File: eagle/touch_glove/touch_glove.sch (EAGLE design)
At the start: 0 parts

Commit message: Added PWM driver and DEMUX to both robotic arm and touch glove.  Added some transistors to touch glove
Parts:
- added C1: CAP_CER_SMD-805_0.1UF-50V-10%, MrSwirlyEyes:CAP_CER_SMD-805_0.1UF-50V-10%
- added C2: CAP_CER_SMD-805_10UF-25V-10%, MrSwirlyEyes:CAP_CER_SMD-805_10UF-25V-10%
- added DEMUX: CD74HC4067-SM96_16:1_MUX-DEMUX, MrSwirlyEyes:CD74HC4067-SM96_16:1_MUX-DEMUX
- added PWM_DRIVER: PCA9685_16-CH_12-BIT_PWM-DRIVER, MrSwirlyEyes:PCA9685_16-CH_12-BIT_PWM-DRIVER
- added R1, R2, R3, R4, R5: RES_SMD-805_10K-5%-1/8W, MrSwirlyEyes:RES_SMD-805_10K-5%-1/8W
- added U1: DRV8830, SparkFun-Retired:DRV8830
- added VIBE_T1, VIBE_T2, VIBE_T3, VIBE_T4, VIBE_T5: SI2302CDS-MOSFET-N-CH_2.6A_20V_57MΩ_SOT23-3, MrSwirlyEyes:SI2302CDS-MOSFET-N-CH_2.6A_20V_57MΩ_SOT23-3
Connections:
- new net C10: DEMUX.C10
- new net C11: DEMUX.C11
- new net C12: DEMUX.C12
- new net C13: DEMUX.C13
- new net C14: DEMUX.C14
- new net C15: DEMUX.C15
- new net C5: DEMUX.C5
- new net C6: DEMUX.C6
- new net C7: DEMUX.C7
- new net C8: DEMUX.C8
- new net C9: DEMUX.C9
- new net GND: C1.2, C2.2, DEMUX.!E, DEMUX.GND, PWM_DRIVER.!OE, PWM_DRIVER.A0, PWM_DRIVER.A1, PWM_DRIVER.A2, PWM_DRIVER.A3, PWM_DRIVER.A4, PWM_DRIVER.A5, PWM_DRIVER.EXTCLK, PWM_DRIVER.GND, R1.1, R2.1, R3.1, R4.1, R5.1, VIBE_T1.S, VIBE_T2.S, VIBE_T3.S, VIBE_T4.S, VIBE_T5.S
- new net PWM10: PWM_DRIVER.PWM10
- new net S0: DEMUX.S0
- new net S1: DEMUX.S1
- new net S2: DEMUX.S2
- new net S3: DEMUX.S3
- new net SCL: PWM_DRIVER.SCL
- new net SDA: PWM_DRIVER.SDA
- new net SIG: DEMUX.SIG
- new net STRAIN_1: DEMUX.C0
- new net STRAIN_2: DEMUX.C1
- new net STRAIN_3: DEMUX.C2
- new net STRAIN_4: DEMUX.C3
- new net STRAIN_5: DEMUX.C4
- new net TEC_1_COLD: PWM_DRIVER.PWM1
- new net TEC_1_HOT: PWM_DRIVER.PWM0
- new net TEC_2_COLD: PWM_DRIVER.PWM3
- new net TEC_2_HOT: PWM_DRIVER.PWM2
- new net TEC_3_COLD: PWM_DRIVER.PWM5
- new net TEC_3_HOT: PWM_DRIVER.PWM4
- new net TEC_4_COLD: PWM_DRIVER.PWM7
- new net TEC_4_HOT: PWM_DRIVER.PWM6
- new net TEC_5_COLD: PWM_DRIVER.PWM9
- new net TEC_5_HOT: PWM_DRIVER.PWM8
- new net VCC: C1.1, C2.1, DEMUX.VCC, PWM_DRIVER.VCC, VIBE_T1.D, VIBE_T2.D, VIBE_T3.D, VIBE_T4.D, VIBE_T5.D
- new net VIBE_1: PWM_DRIVER.PWM11, R1.2, VIBE_T1.G
- new net VIBE_2: PWM_DRIVER.PWM12, R2.2, VIBE_T2.G
- new net VIBE_3: PWM_DRIVER.PWM13, R3.2, VIBE_T3.G
- new net VIBE_4: PWM_DRIVER.PWM14, R4.2, VIBE_T4.G
- new net VIBE_5: PWM_DRIVER.PWM15, R5.2, VIBE_T5.G
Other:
- note added: "DEMUX for STRAIN SENSORS"
- note added: "I2C ADDR: x40"
- note added: "PWM DRIVER [TEC + VIBE]"
- note added: "VIBE MOTOR DRIVERS"
- note removed: "INITIALIZING touch_glove"

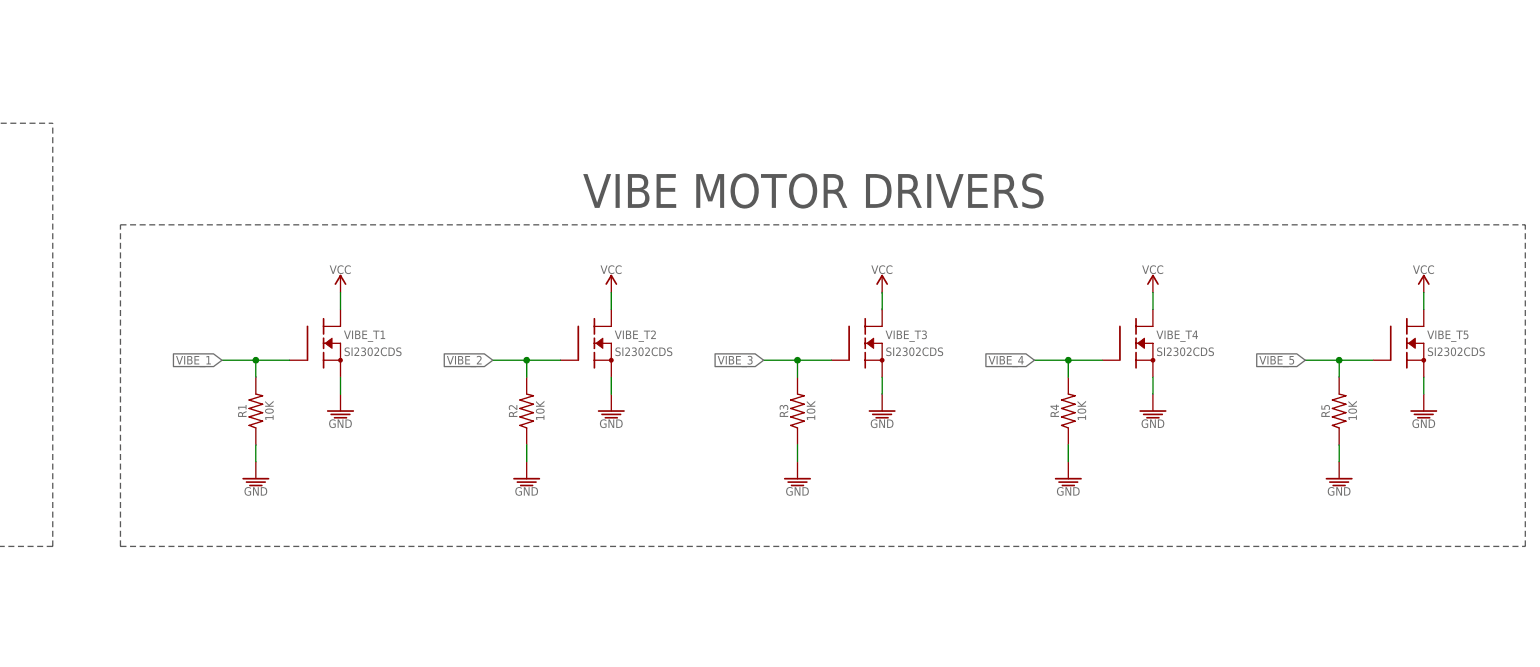
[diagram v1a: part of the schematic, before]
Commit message: Added vibe motor plus transistor driver arrangement
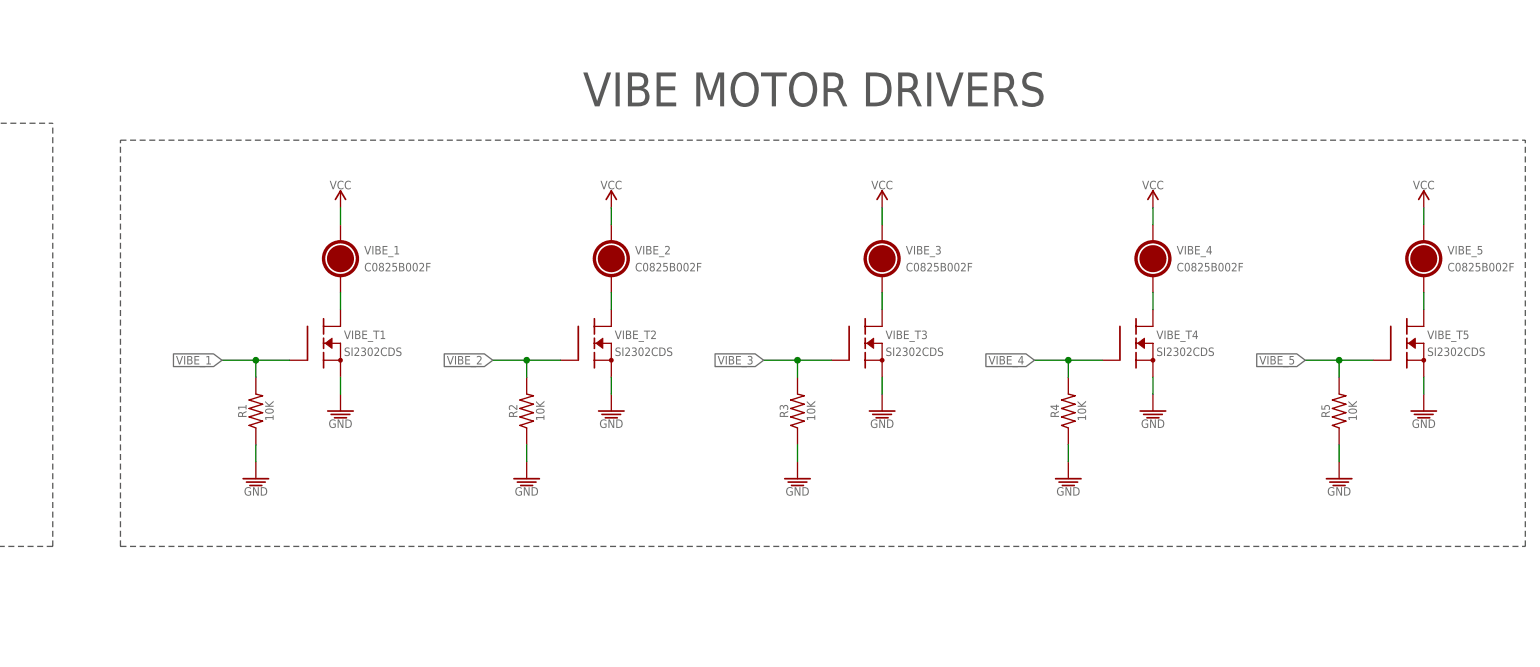
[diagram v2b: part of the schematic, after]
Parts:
- added VIBE_1, VIBE_2, VIBE_3, VIBE_4, VIBE_5: VIBE_MOTOR, MrSwirlyEyes:VIBE_MOTOR
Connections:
- new net N$1: VIBE_1.-, VIBE_T1.D
- new net N$2: VIBE_5.-, VIBE_T5.D
- new net N$3: VIBE_4.-, VIBE_T4.D
- new net N$4: VIBE_3.-, VIBE_T3.D
- new net N$5: VIBE_2.-, VIBE_T2.D
- net VCC: now also VIBE_1.+, VIBE_2.+, VIBE_3.+, VIBE_4.+, VIBE_5.+; no longer VIBE_T1.D, VIBE_T2.D, VIBE_T3.D, VIBE_T4.D, VIBE_T5.D
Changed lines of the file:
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@@
 <setting verticaltext="up"/>
 </settings>
-<grid distance="0.1" unitdist="inch" unit="inch" style="lines" multiple="1" display="yes" altdistance="0.05" altunitdist="inch" altunit="inch"/>
+<grid distance="0.1" unitdist="inch" unit="inch" style="lines" multiple="1" display="yes" altdistance="0.01" altunitdist="inch" altunit="inch"/>
 <layers>
 <layer number="1" name="Top" color="4" fill="1" visible="no" active="no"/>
@@
 <part name="R5" library="MrSwirlyEyes" deviceset="RES_SMD-805_10K-5%-1/8W" device=""/>
 <part name="GND14" library="MrSwirlyEyes" deviceset="GND" device=""/>
+<part name="VIBE_1" library="MrSwirlyEyes" deviceset="VIBE_MOTOR" device=""/>
+<part name="VIBE_2" library="MrSwirlyEyes" deviceset="VIBE_MOTOR" device=""/>
+<part name="VIBE_3" library="MrSwirlyEyes" deviceset="VIBE_MOTOR" device=""/>
+<part name="VIBE_4" library="MrSwirlyEyes" deviceset="VIBE_MOTOR" device=""/>
+<part name="VIBE_5" library="MrSwirlyEyes" deviceset="VIBE_MOTOR" device=""/>
 </parts>
 <sheets>
@@
 [TEC + VIBE]</text>
 <text x="129.54" y="15.24" size="1.27" layer="91" font="vector" ratio="10">I2C ADDR: x40</text>
-<wire x1="185.42" y1="10.16" x2="185.42" y2="58.42" width="0.1524" layer="97" style="shortdash"/>
-<wire x1="396.24" y1="10.16" x2="396.24" y2="58.42" width="0.1524" layer="97" style="shortdash"/>
-<wire x1="185.42" y1="58.42" x2="396.24" y2="58.42" width="0.1524" layer="97" style="shortdash"/>
+<wire x1="185.42" y1="10.16" x2="185.42" y2="71.12" width="0.1524" layer="97" style="shortdash"/>
+<wire x1="396.24" y1="10.16" x2="396.24" y2="71.12" width="0.1524" layer="97" style="shortdash"/>
+<wire x1="185.42" y1="71.12" x2="396.24" y2="71.12" width="0.1524" layer="97" style="shortdash"/>
 <wire x1="185.42" y1="10.16" x2="396.24" y2="10.16" width="0.1524" layer="97" style="shortdash"/>
-<text x="289.56" y="63.5" size="5.08" layer="97" font="vector" ratio="20" align="center">VIBE MOTOR DRIVERS</text>
+<text x="289.56" y="78.74" size="5.08" layer="97" font="vector" ratio="20" align="center">VIBE MOTOR DRIVERS</text>
 </plain>
 <instances>
@@
 <instance part="GND5" gate="GND" x="218.44" y="30.48"/>
 <instance part="SUPPLY2" gate="VCC" x="104.14" y="63.5"/>
-<instance part="SUPPLY3" gate="VCC" x="218.44" y="48.26"/>
+<instance part="SUPPLY3" gate="VCC" x="218.44" y="60.96"/>
 <instance part="R1" gate="G$1" x="205.74" y="30.48" rot="R90"/>
 <instance part="GND6" gate="GND" x="205.74" y="20.32"/>
 <instance part="VIBE_T2" gate="G$1" x="256.54" y="40.64"/>
 <instance part="GND7" gate="GND" x="259.08" y="30.48"/>
-<instance part="SUPPLY4" gate="VCC" x="259.08" y="48.26"/>
+<instance part="SUPPLY4" gate="VCC" x="259.08" y="60.96"/>
 <instance part="R2" gate="G$1" x="246.38" y="30.48" rot="R90"/>
 <instance part="GND8" gate="GND" x="246.38" y="20.32"/>
 <instance part="VIBE_T3" gate="G$1" x="297.18" y="40.64"/>
 <instance part="GND9" gate="GND" x="299.72" y="30.48"/>
-<instance part="SUPPLY5" gate="VCC" x="299.72" y="48.26"/>
+<instance part="SUPPLY5" gate="VCC" x="299.72" y="60.96"/>
 <instance part="R3" gate="G$1" x="287.02" y="30.48" rot="R90"/>
 <instance part="GND10" gate="GND" x="287.02" y="20.32"/>
 <instance part="VIBE_T4" gate="G$1" x="337.82" y="40.64"/>
 <instance part="GND11" gate="GND" x="340.36" y="30.48"/>
-<instance part="SUPPLY6" gate="VCC" x="340.36" y="48.26"/>
+<instance part="SUPPLY6" gate="VCC" x="340.36" y="60.96"/>
 <instance part="R4" gate="G$1" x="327.66" y="30.48" rot="R90"/>
 <instance part="GND12" gate="GND" x="327.66" y="20.32"/>
 <instance part="VIBE_T5" gate="G$1" x="378.46" y="40.64"/>
 <instance part="GND13" gate="GND" x="381" y="30.48"/>
-<instance part="SUPPLY7" gate="VCC" x="381" y="48.26"/>
+<instance part="SUPPLY7" gate="VCC" x="381" y="60.96"/>
 <instance part="R5" gate="G$1" x="368.3" y="30.48" rot="R90"/>
 <instance part="GND14" gate="GND" x="368.3" y="20.32"/>
+<instance part="VIBE_1" gate="G$1" x="218.44" y="53.34"/>
+<instance part="VIBE_2" gate="G$1" x="259.08" y="53.34"/>
+<instance part="VIBE_3" gate="G$1" x="299.72" y="53.34"/>
+<instance part="VIBE_4" gate="G$1" x="340.36" y="53.34"/>
+<instance part="VIBE_5" gate="G$1" x="381" y="53.34"/>
 </instances>
 <busses>
@@
 </segment>
 <segment>
-<pinref part="VIBE_T1" gate="G$1" pin="D"/>
-<wire x1="218.44" y1="45.72" x2="218.44" y2="48.26" width="0.1524" layer="91"/>
+<pinref part="VIBE_1" gate="G$1" pin="+"/>
 <pinref part="SUPPLY3" gate="VCC" pin="VCC"/>
-</segment>
-<segment>
-<pinref part="VIBE_T2" gate="G$1" pin="D"/>
-<wire x1="259.08" y1="45.72" x2="259.08" y2="48.26" width="0.1524" layer="91"/>
+<wire x1="218.44" y1="58.42" x2="218.44" y2="60.96" width="0.1524" layer="91"/>
+</segment>
+<segment>
+<pinref part="SUPPLY7" gate="VCC" pin="VCC"/>
+<pinref part="VIBE_5" gate="G$1" pin="+"/>
+<wire x1="381" y1="60.96" x2="381" y2="58.42" width="0.1524" layer="91"/>
+</segment>
+<segment>
+<pinref part="VIBE_4" gate="G$1" pin="+"/>
+<pinref part="SUPPLY6" gate="VCC" pin="VCC"/>
+<wire x1="340.36" y1="58.42" x2="340.36" y2="60.96" width="0.1524" layer="91"/>
+</segment>
+<segment>
+<pinref part="SUPPLY5" gate="VCC" pin="VCC"/>
+<pinref part="VIBE_3" gate="G$1" pin="+"/>
+<wire x1="299.72" y1="60.96" x2="299.72" y2="58.42" width="0.1524" layer="91"/>
+</segment>
+<segment>
 <pinref part="SUPPLY4" gate="VCC" pin="VCC"/>
-</segment>
-<segment>
-<pinref part="VIBE_T3" gate="G$1" pin="D"/>
-<wire x1="299.72" y1="45.72" x2="299.72" y2="48.26" width="0.1524" layer="91"/>
-<pinref part="SUPPLY5" gate="VCC" pin="VCC"/>
-</segment>
-<segment>
-<pinref part="VIBE_T4" gate="G$1" pin="D"/>
-<wire x1="340.36" y1="45.72" x2="340.36" y2="48.26" width="0.1524" layer="91"/>
-<pinref part="SUPPLY6" gate="VCC" pin="VCC"/>
-</segment>
-<segment>
-<pinref part="VIBE_T5" gate="G$1" pin="D"/>
-<wire x1="381" y1="45.72" x2="381" y2="48.26" width="0.1524" layer="91"/>
-<pinref part="SUPPLY7" gate="VCC" pin="VCC"/>
+<pinref part="VIBE_2" gate="G$1" pin="+"/>
+<wire x1="259.08" y1="60.96" x2="259.08" y2="58.42" width="0.1524" layer="91"/>
 </segment>
 </net>
@@
 </segment>
 </net>
+<net name="N$1" class="0">
+<segment>
+<pinref part="VIBE_T1" gate="G$1" pin="D"/>
+<pinref part="VIBE_1" gate="G$1" pin="-"/>
+<wire x1="218.44" y1="48.26" x2="218.44" y2="45.72" width="0.1524" layer="91"/>
+</segment>
+</net>
+<net name="N$2" class="0">
+<segment>
+<pinref part="VIBE_5" gate="G$1" pin="-"/>
+<pinref part="VIBE_T5" gate="G$1" pin="D"/>
+<wire x1="381" y1="48.26" x2="381" y2="45.72" width="0.1524" layer="91"/>
+</segment>
+</net>
+<net name="N$3" class="0">
+<segment>
+<pinref part="VIBE_T4" gate="G$1" pin="D"/>
+<pinref part="VIBE_4" gate="G$1" pin="-"/>
+<wire x1="340.36" y1="45.72" x2="340.36" y2="48.26" width="0.1524" layer="91"/>
+</segment>
+</net>
+<net name="N$4" class="0">
+<segment>
+<pinref part="VIBE_T3" gate="G$1" pin="D"/>
+<pinref part="VIBE_3" gate="G$1" pin="-"/>
+<wire x1="299.72" y1="45.72" x2="299.72" y2="48.26" width="0.1524" layer="91"/>
+</segment>
+</net>
+<net name="N$5" class="0">
+<segment>
+<pinref part="VIBE_2" gate="G$1" pin="-"/>
+<pinref part="VIBE_T2" gate="G$1" pin="D"/>
+<wire x1="259.08" y1="48.26" x2="259.08" y2="45.72" width="0.1524" layer="91"/>
+</segment>
+</net>

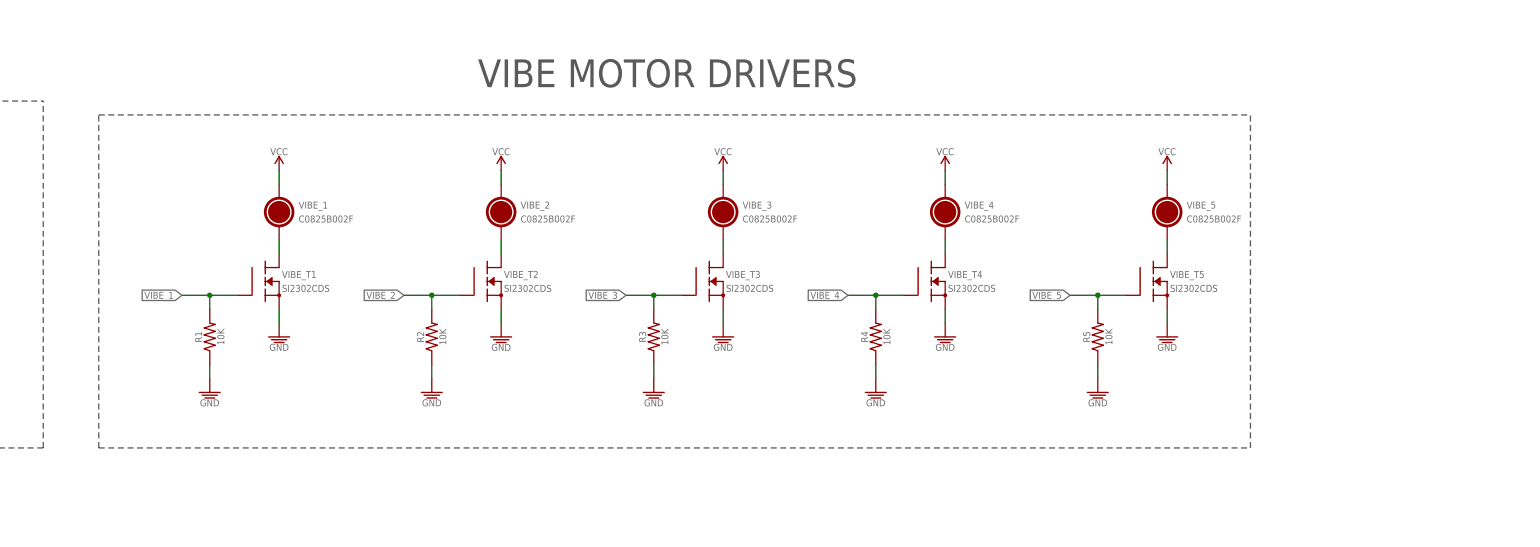
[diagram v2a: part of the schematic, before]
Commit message: Added diode and cap to Touch Glove vibe motor drivers
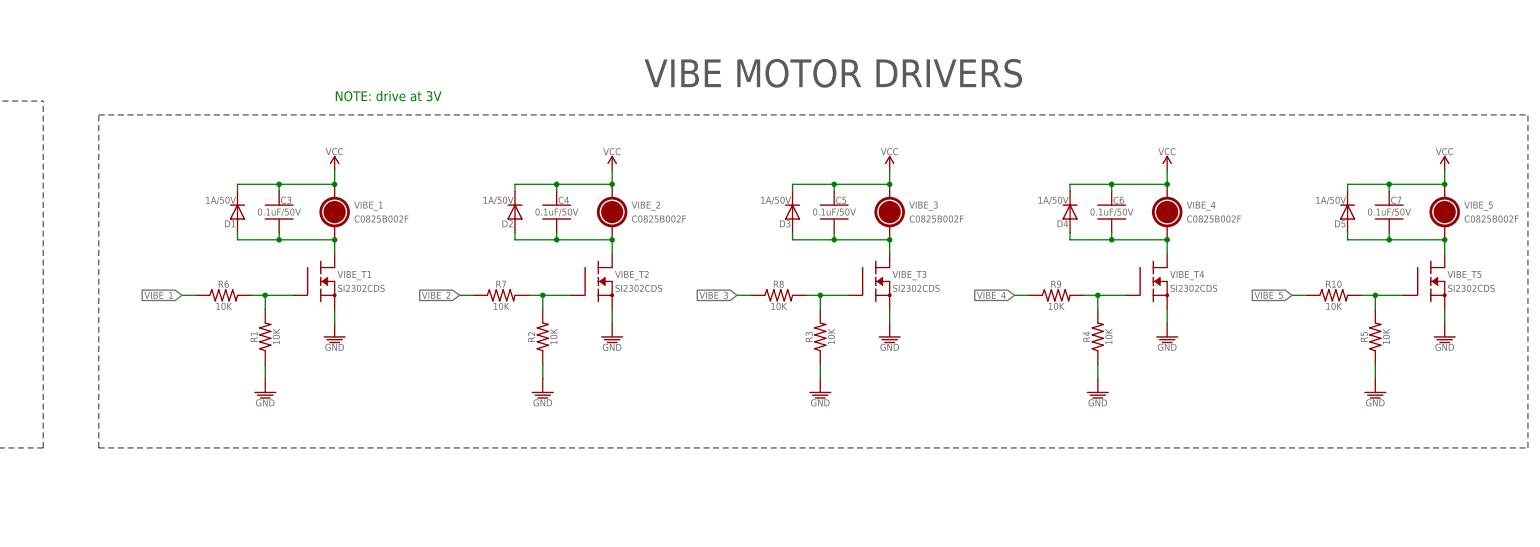
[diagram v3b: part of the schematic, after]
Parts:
- added C3, C4, C5, C6, C7: CAP_CER_SMD-805_0.1UF-50V-10%, MrSwirlyEyes:CAP_CER_SMD-805_0.1UF-50V-10%
- added D1, D2, D3, D4, D5: DIODE_SMD_GP_1A-50V-SOD123F, MrSwirlyEyes:DIODE_SMD_GP_1A-50V-SOD123F
- added R10, R6, R7, R8, R9: RES_SMD-805_10K-5%-1/8W, MrSwirlyEyes:RES_SMD-805_10K-5%-1/8W
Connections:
- removed net N$2: VIBE_5.-, VIBE_T5.D
- removed net N$5: VIBE_2.-, VIBE_T2.D
- new net N$10: R7.1
- new net N$11: C4.2, D2.A, VIBE_2.-, VIBE_T2.D
- new net N$14: C7.2, D5.A, VIBE_5.-, VIBE_T5.D
- new net N$6: R6.1
- new net N$7: R10.1
- new net N$8: R9.1
- new net N$9: R8.1
- net N$1: now also C3.2, D1.A
- net N$3: now also C6.2, D4.A
- net N$4: now also C5.2, D3.A
- net VCC: now also C3.1, C4.1, C5.1, C6.1, C7.1, D1.K, D2.K, D3.K, D4.K, D5.K
- net VIBE_1: now also R6.2
- net VIBE_2: now also R7.2
- net VIBE_3: now also R8.2
- net VIBE_4: now also R9.2
- net VIBE_5: now also R10.2
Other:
- note added: "NOTE: drive at 3V"
- moved on the sheet: R1, R2, R3, R4, R5, VIBE_1, VIBE_2, VIBE_3, VIBE_4, VIBE_5, VIBE_T1, VIBE_T2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

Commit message: Added Peltier driving circuitry
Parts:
- added C10, C13, C16, C19, C22: CAP_POL_ALUM-ELECTROLYTIC_SMD_100UF-16V-20%, MrSwirlyEyes:CAP_POL_ALUM-ELECTROLYTIC_SMD_100UF-16V-20%
- added C11, C12, C14, C15, C17, C18, C20, C21, C8, C9: CAP_CER_SMD-805_0.1UF-50V-10%, MrSwirlyEyes:CAP_CER_SMD-805_0.1UF-50V-10%
- added P1, P2, P3, P4, P5: PELTIER-CM23-1.9-05AC_1.9A-2.8V_8X6X2MM, MrSwirlyEyes:PELTIER-CM23-1.9-05AC_1.9A-2.8V_8X6X2MM
- added U2, U3, U4, U5, U6: DRV8837C_H-BRIDGE_1A_WSON-8-PAD, MrSwirlyEyes:DRV8837C_H-BRIDGE_1A_WSON-8-PAD
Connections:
- new net N$1: P2.HOT, U3.OUT1
- new net N$11: P3.HOT, U4.OUT1
- new net N$12: P3.COLD, U4.OUT2
- new net N$13: P1.HOT, U2.OUT1
- new net N$14: P1.COLD, U2.OUT2
- new net N$16: P4.HOT, U5.OUT1
- new net N$18: P4.COLD, U5.OUT2
- new net N$19: P5.HOT, U6.OUT1
- new net N$20: P5.COLD, U6.OUT2
- new net N$5: P2.COLD, U3.OUT2
- net GND: now also C10.K, C11.2, C12.2, C13.K, C14.2, C15.2, C16.K, C17.2, C18.2, C19.K, C20.2, C21.2, C22.K, C8.2, C9.2, DEMUX.!EN, U2.GND, U3.GND, U4.GND, U5.GND, U6.GND; no longer DEMUX.!E
- net TEC_1_COLD: now also U2.IN2
- net TEC_1_HOT: now also U2.IN1
- net TEC_2_COLD: now also U3.IN2
- net TEC_2_HOT: now also U3.IN1
- net TEC_3_COLD: now also U4.IN2
- net TEC_3_HOT: now also U4.IN1
- net TEC_4_COLD: now also U5.IN2
- net TEC_4_HOT: now also U5.IN1
- net TEC_5_COLD: now also U6.IN2
- net TEC_5_HOT: now also U6.IN1
- net VCC: now also C10.A, C11.1, C12.1, C13.A, C14.1, C15.1, C16.A, C17.1, C18.1, C19.A, C20.1, C21.1, C22.A, C8.1, C9.1, U2.NSLEEP, U2.VCC, U2.VM, U3.NSLEEP, U3.VCC, U3.VM, U4.NSLEEP, U4.VCC, U4.VM, U5.NSLEEP, U5.VCC, U5.VM, U6.NSLEEP, U6.VCC, U6.VM
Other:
- note added: "CHANGE TO VBATT or VM"
- note added: "PELTIER DRIVERS"
- moved on the sheet: R1, R10, R2, R3, R4, R5, R6, R7, R8, R9, U1, VIBE_T1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

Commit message: Modfied git ignore.  Added h bridge files.  Modified EAGLE files
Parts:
- removed U1: DRV8830, SparkFun-Retired:DRV8830
- added F1: FSR, MrSwirlyEyes:FSR_FORCE-SENSATIVE-RESISTOR_PRESS-SENSOR
- added R11: 10KΩ, MrSwirlyEyes:RESISTORSMD-0805_1/8W_10K_5%
- C1, C11, C12, C14, C15, C17, C18, C20, C21, C3, C4, C5, C6, C7, C8, C9: value CAP_CER_SMD-805_0.1UF-50V-10% -> 0.1uF/50V; device MrSwirlyEyes:CAP_CER_SMD-805_0.1UF-50V-10% -> MrSwirlyEyes:CAPACITOR_CERAMIC_SMD-805_0.1UF-50V-10%
- C10, C13, C16, C19, C22: value CAP_POL_ALUM-ELECTROLYTIC_SMD_100UF-16V-20% -> 100UF/16V; device MrSwirlyEyes:CAP_POL_ALUM-ELECTROLYTIC_SMD_100UF-16V-20% -> MrSwirlyEyes:CAPACITOR_POLARIZED_ALUM-ELECTROLYTIC_SMD_100UF-16V-20%
- C2: value CAP_CER_SMD-805_10UF-25V-10% -> 10uF/25V; device MrSwirlyEyes:CAP_CER_SMD-805_10UF-25V-10% -> MrSwirlyEyes:CAPACITOR_CERAMIC_SMD-805_10UF-25V-10%
- D1, D2, D3, D4, D5: value DIODE_SMD_GP_1A-50V-SOD123F -> 1A/50V
- DEMUX: value CD74HC4067-SM96_16:1_MUX-DEMUX -> CH16_MUX-DEMUX
- P1, P2, P3, P4, P5: value PELTIER-CM23-1.9-05AC_1.9A-2.8V_8X6X2MM -> PELTIER
- PWM_DRIVER: value PCA9685_16-CH_12-BIT_PWM-DRIVER -> PCA9685
- R1, R10, R2, R3, R4, R5, R6, R7, R8, R9: value RES_SMD-805_10K-5%-1/8W -> 10KΩ; device MrSwirlyEyes:RES_SMD-805_10K-5%-1/8W -> MrSwirlyEyes:RESISTORSMD-0805_1/8W_10K_5%
- U2, U3, U4, U5, U6: value DRV8837C_H-BRIDGE_1A_WSON-8-PAD -> DRV8837C
- VIBE_1, VIBE_2, VIBE_3, VIBE_4, VIBE_5: device MrSwirlyEyes:VIBE_MOTOR -> MrSwirlyEyes:VIBE_MOTOR_100MA/3V
- VIBE_T1, VIBE_T2, VIBE_T3, VIBE_T4, VIBE_T5: value SI2302CDS-MOSFET-N-CH_2.6A_20V_57MΩ_SOT23-3 -> 2.6A/20V/57mΩ; device MrSwirlyEyes:SI2302CDS-MOSFET-N-CH_2.6A_20V_57MΩ_SOT23-3 -> MrSwirlyEyes:MOSFET-N-CH_SI2302CDS_2.6A_20V_57MΩ_SOT23-3
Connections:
- removed net C15: DEMUX.C15
- new net FSR_1: DEMUX.C15, F1.-, R11.2
- net GND: now also R11.1
- net VCC: now also F1.+
